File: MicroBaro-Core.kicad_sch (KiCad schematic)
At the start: 27 parts, among them J1 USB_C_Receptacle_USB2.0_16P, J2 Micro_SD_Card, J3 Conn_01x04, J4 Conn_01x02, U1 ATSAMD21E16B-MU, U2 BMP390, U3 BMI160, U4 TPS3839DBZ, U5 TPTLV73333PDBVR, Y1 12MHz

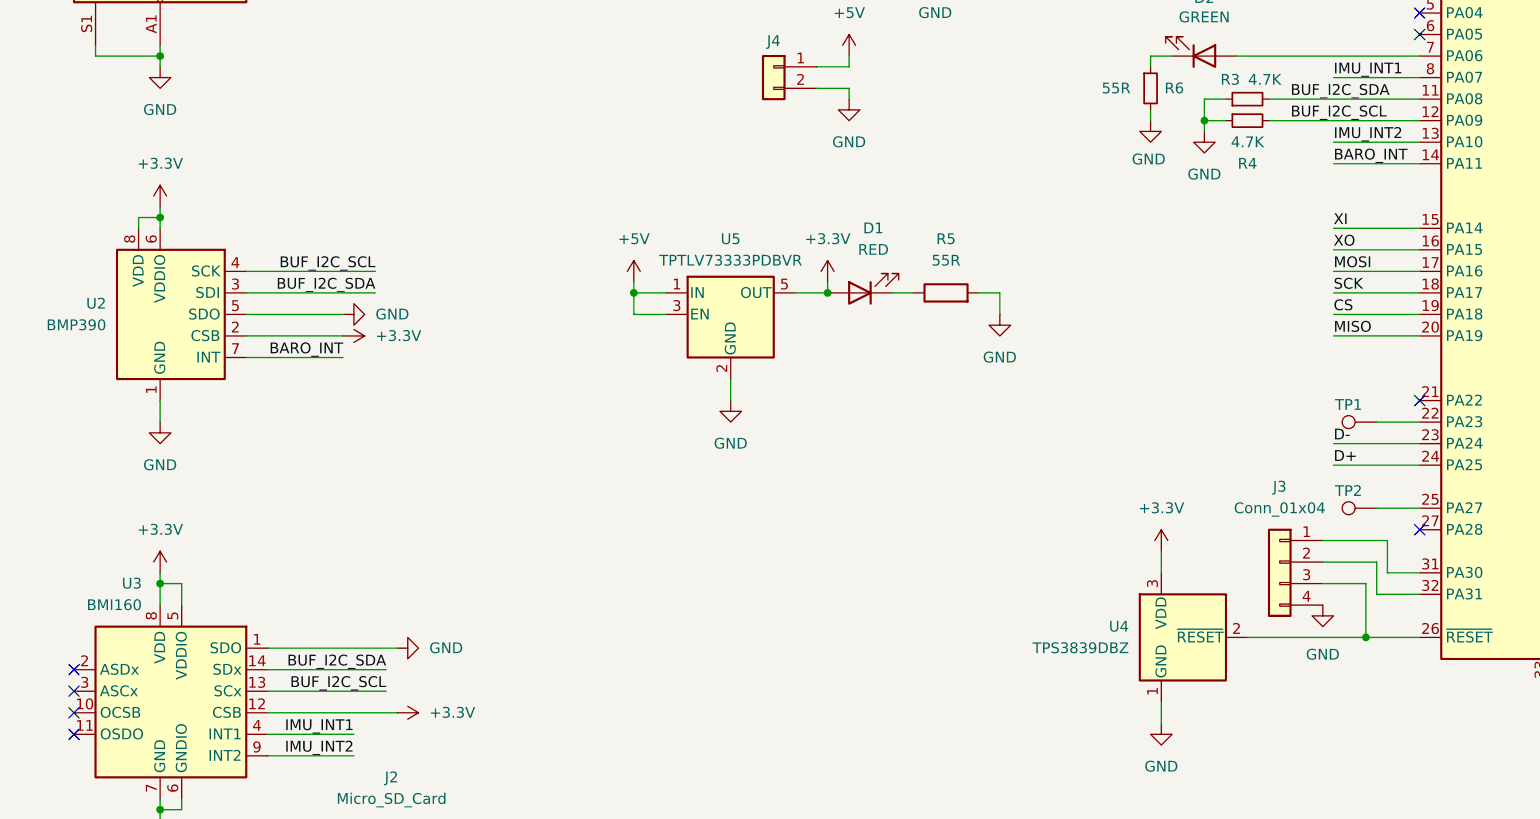
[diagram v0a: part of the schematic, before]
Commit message: Add BMP390 symbols
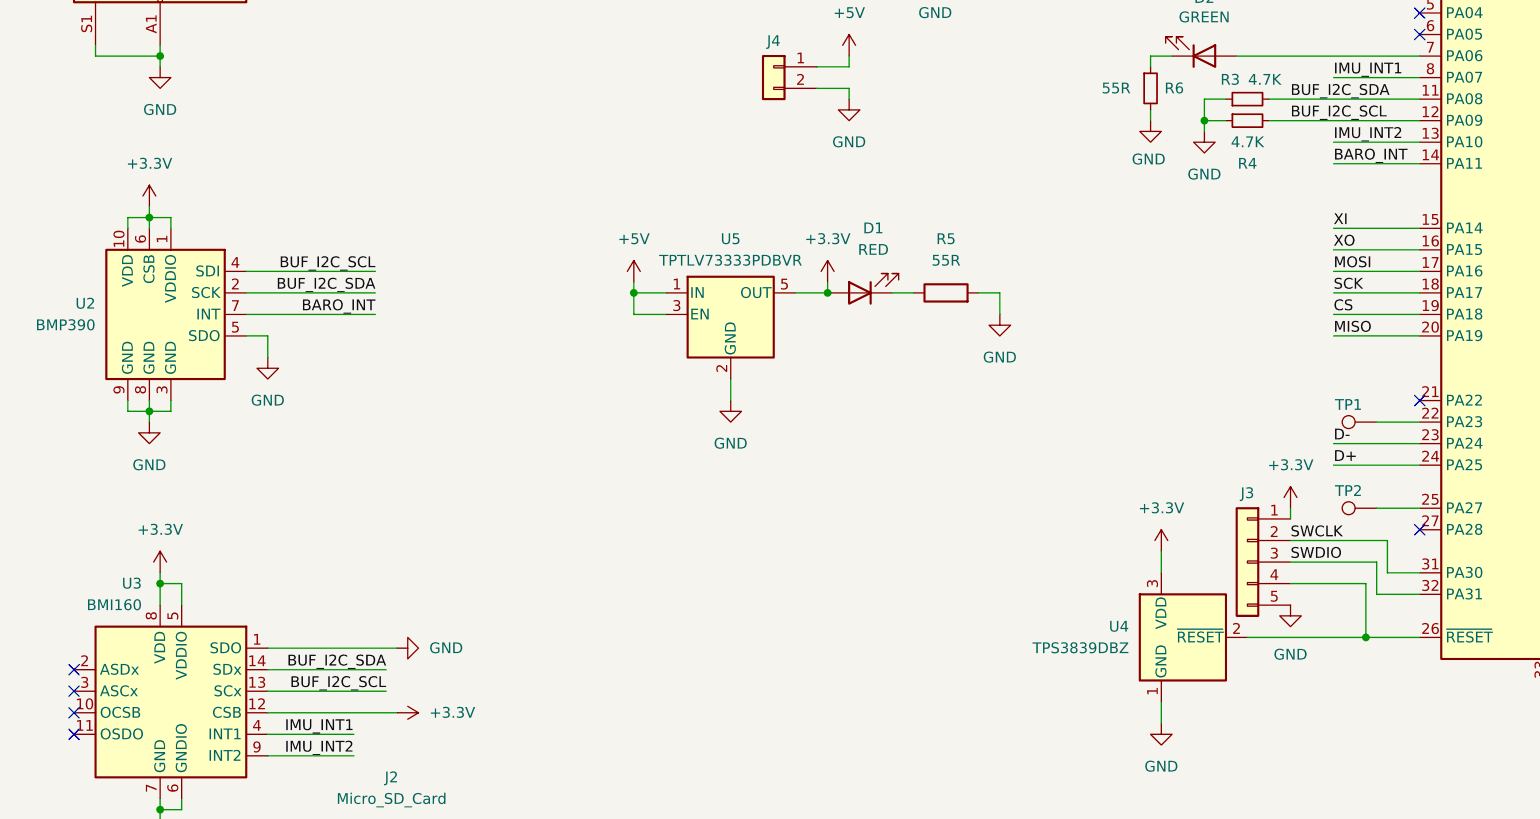
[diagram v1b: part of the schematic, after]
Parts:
- J3: footprint Connector_PinHeader_2.54mm:PinHeader_1x04_P2.54mm_Vertical -> Connector_PinHeader_2.54mm:PinHeader_1x05_P2.54mm_Vertical; symbol Connector_Generic:Conn_01x04 -> Connector_Generic:Conn_01x05; now in the parts list
- U2: footprint Package_LGA:Bosch_LGA-8_2x2.5mm_P0.65mm_ClockwisePinNumbering -> Project:Bosch_WFLGA-10_2x2mm_P0.5mm
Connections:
- net +3.3V: now also J3.1 (Pin_1), U2.1 (VDDIO), U2.10 (VDD); no longer U2.2 (CSB), U2.8 (VDD)
- net BUF_I2C_SDA: now also U2.2 (SCK); no longer U2.3 (SDI)
- net GND: now also J3.5 (Pin_5), U2.3 (GND), U2.8 (GND), U2.9 (GND); no longer J3.4 (Pin_4), U2.1 (GND)
- net at U1.26 (~{RESET}), U4.2 (~{RESET}): now also J3.4 (Pin_4); no longer J3.3 (Pin_3)
- net SWCLK: now reaches U1.31 (PA30)
- net SWCLK: now also J3.2 (Pin_2); no longer J3.1 (Pin_1)
- net SWDIO: now reaches U1.32 (PA31)
- net SWDIO: now also J3.3 (Pin_3); no longer J3.2 (Pin_2)

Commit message: Next revision
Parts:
- removed U4: TPS3839DBZ, Package_TO_SOT_SMD:SOT-23, symbol Power_Supervisor:TPS3839DBZ
- added JP1: SolderJumper_2_Open, Jumper:SolderJumper-2_P1.3mm_Open_RoundedPad1.0x1.5mm, symbol Jumper:SolderJumper_2_Open
- added U6: TPS3831, Package_SON:Texas_X2SON-4_1x1mm_P0.65mm, symbol Power_Supervisor:TPS3831
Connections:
- net +3.3V: now also U6.4 (VDD)
- net CS: now also U1.6 (PA05); no longer U1.19 (PA18)
- net GND: now also JP1.1 (A), U6.3 (GND)
- net XI: now also U1.1 (PA00); no longer U1.15 (PA14)
- net XO: now also U1.2 (PA01); no longer U1.16 (PA15)
- net at U1.26 (~{RESET}): now also U6.1 (~{RESET}); no longer J3.4 (Pin_4)
- net at D2.2 (A): now also U1.16 (PA15); no longer U1.7 (PA06)
- new net MR: J3.4 (Pin_4), JP1.2 (B), U6.2 (~{MR})
- no-connect marks 16 -> 17
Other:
- moved on the sheet: D2, R6

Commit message: Next revision
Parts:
- removed R3, R4: 4.7K, Resistor_SMD:R_0603_1608Metric, symbol Device:R_Small
- added C4, C5, C6: 0.1uF, Capacitor_SMD:C_0603_1608Metric, symbol Device:C_Small
- J1: LCSC Part # (none) -> C3025063
- J3: now left out of the parts list
- U6: DigiKey Part # (none) -> 296-40752-1-ND; LCSC Part # (none) -> C544470; MPN (none) -> TPS3831K33DQNR; Manufacturer (none) -> Texas Instruments
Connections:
- net +3.3V: now also C5.1, C6.1
- net BUF_I2C_SCL: now also U2.2 (SCK); no longer U2.4 (SDI)
- net BUF_I2C_SDA: now also U2.4 (SDI); no longer U2.2 (SCK)
- net GND: now also C4.1, C5.2, C6.2; no longer U2.3 (GND)
- new net: C4.2, U2.3 (GND)
